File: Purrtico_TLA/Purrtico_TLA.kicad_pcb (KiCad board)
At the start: 2 copper layers, 100 x 50 mm, 67 parts, among them J1 XLR3, J3 Conn_01x02, J4 XLR3, J5 Conn_01x02, J7 Conn_02x05_Odd_Even, U1 OPA1679, U2 OPA1679

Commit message: update circuit
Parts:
- removed RV3: 10k, Connector_PinHeader_2.54mm:PinHeader_1x03_P2.54mm_Vertical
- added R33: 1k, Resistor_SMD:R_1206_3216Metric, F.Cu at (105.9, 75.9)
- R19: value 1k -> 10k
- R7: value 2k2 -> 3k3
- moved R19 1.43 mm to (102.7, 73.2)
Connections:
- R19 pad 2: Net-(U1C--) -> Net-(U1C-+)
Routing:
- net Net-(U1C-+): track 15.4 -> 8.07 mm
- net Net-(C3-Pad1): track 36.6 -> 41.7 mm, vias 4 -> 2
- net Net-(C5-Pad2): track 15.9 -> 13.7 mm
- net Net-(U1C--): track 5.06 -> 2.86 mm

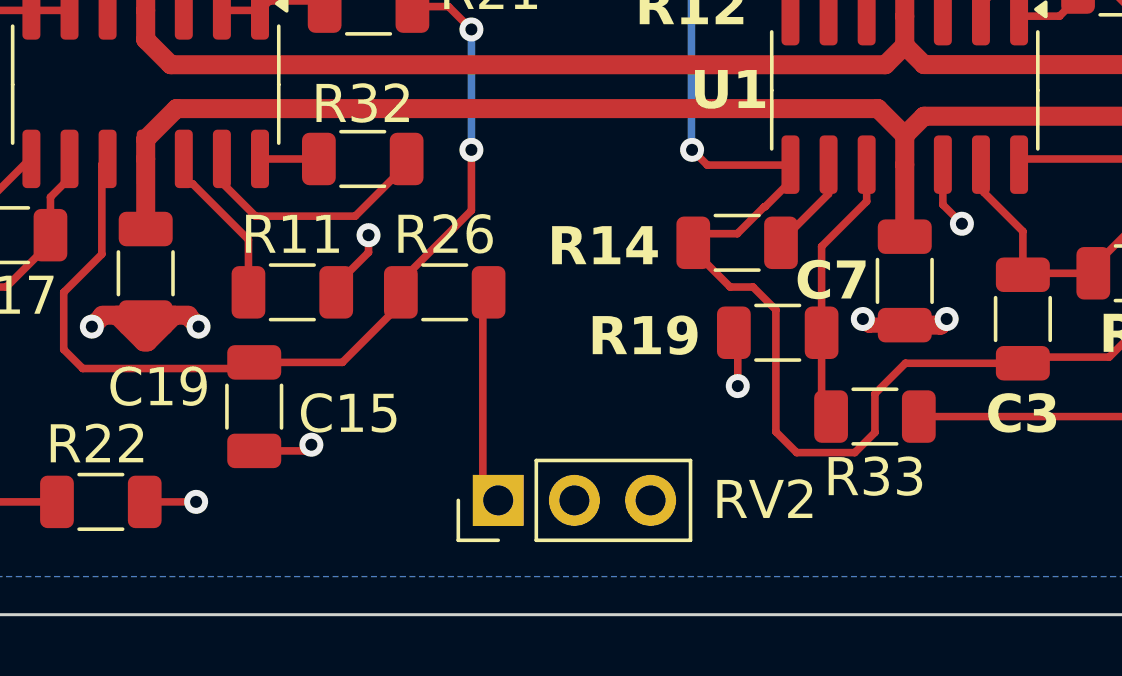
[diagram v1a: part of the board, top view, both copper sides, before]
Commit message: update annotation
parity with final r00
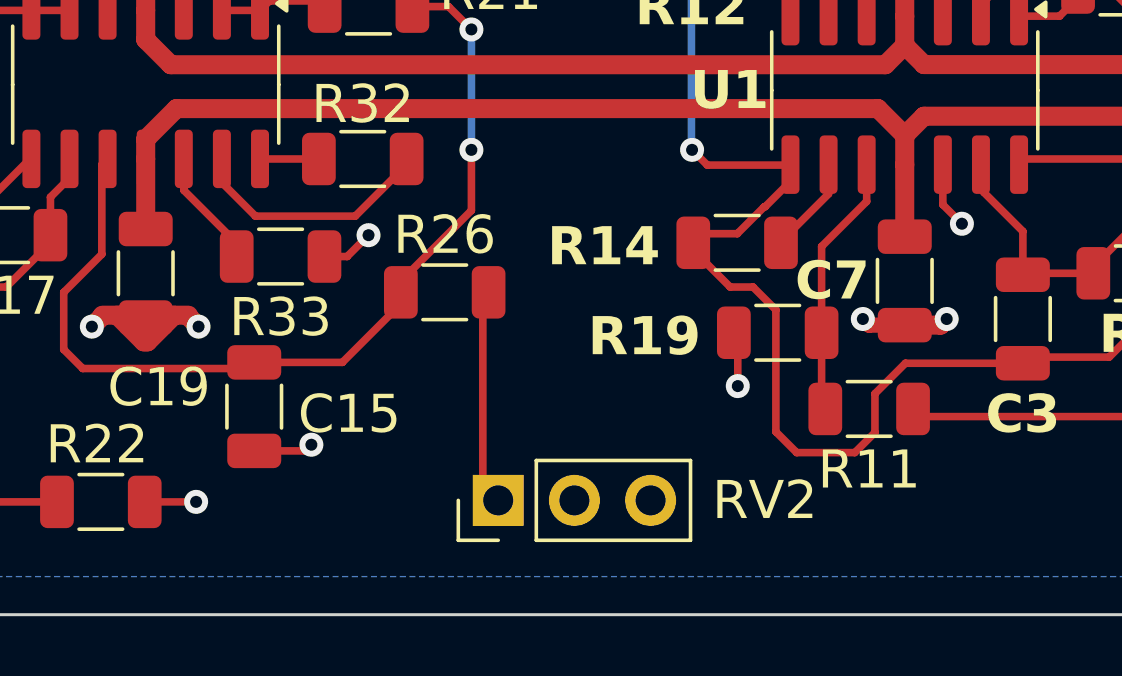
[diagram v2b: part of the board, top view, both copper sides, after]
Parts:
- R11: value 0R -> 1k
- R33: value 1k -> 0R
- moved R33 20.5 mm to (86.1, 70.6)
- moved R11 19.6 mm to (105.7, 75.7)
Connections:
- R11 pad 1: Net-(U2D-+) -> Net-(U1C-+)
- R11 pad 2: GND -> Net-(C5-Pad2)
- R33 pad 1: Net-(U1C-+) -> Net-(U2D-+)
- R33 pad 2: Net-(C5-Pad2) -> GND
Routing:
- net Net-(U2D-+): track 4.68 -> 2.54 mm
